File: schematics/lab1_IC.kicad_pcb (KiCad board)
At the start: 2 copper layers, 67.1 x 68.6 mm, 19 parts, among them J1 Barrel_Jack, M1 Motor_Servo, U1 LM7805_TO220, U2 NodeMCU, U3 DHT11

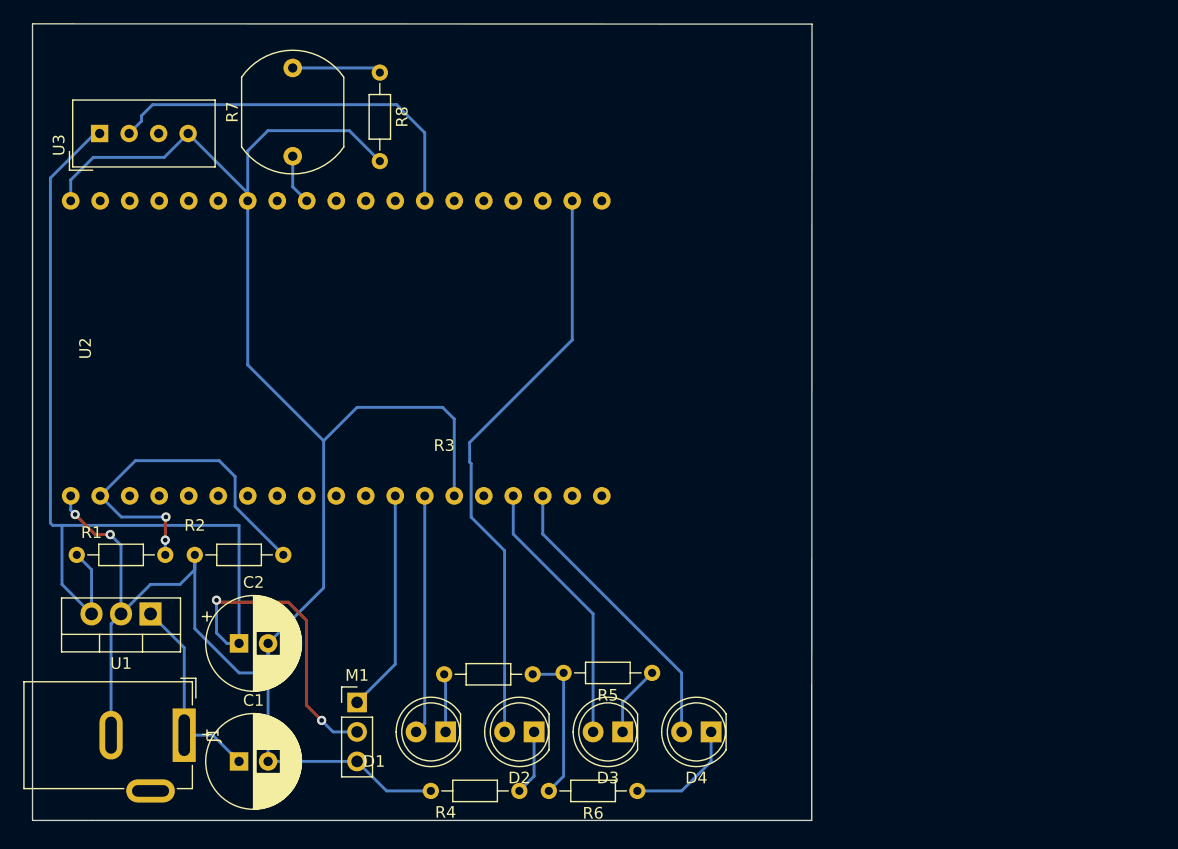
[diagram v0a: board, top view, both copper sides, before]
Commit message: added: servo functions to firmware
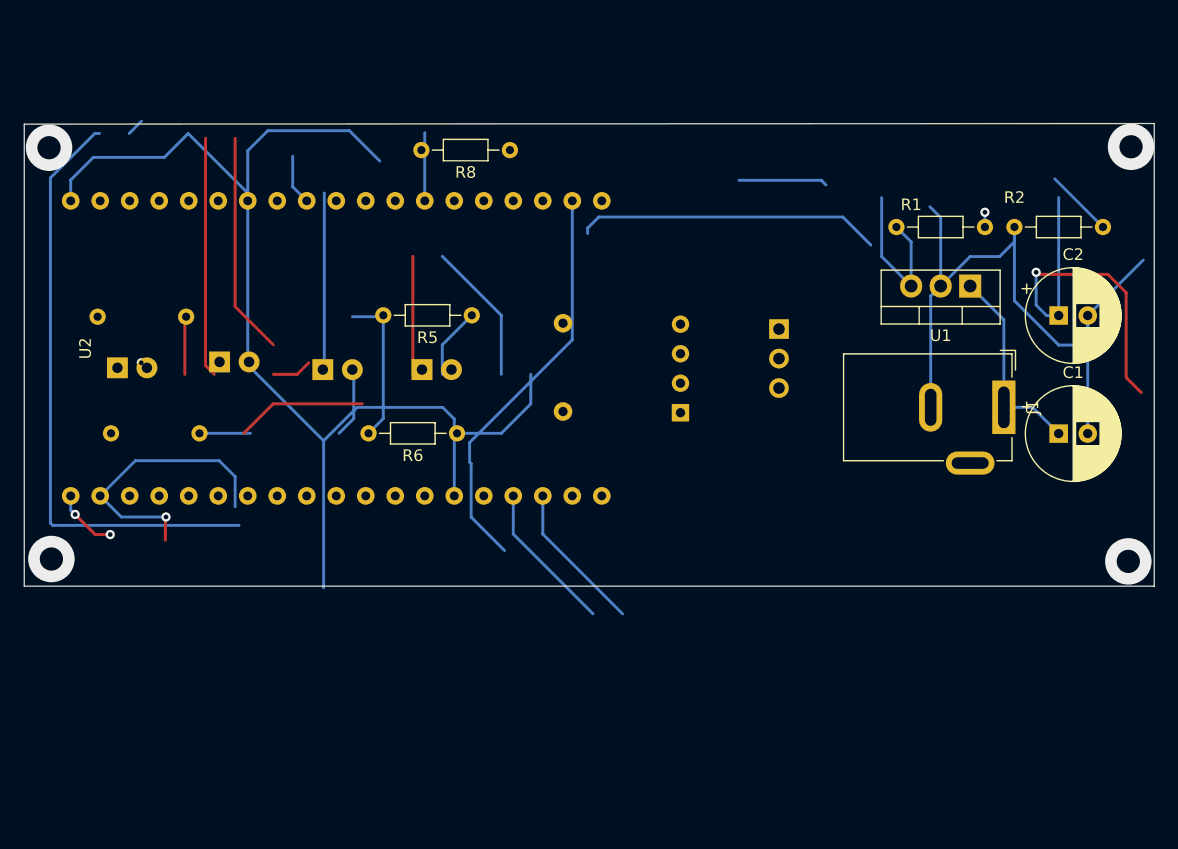
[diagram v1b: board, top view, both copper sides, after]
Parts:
- D1, D2, D3, D4, M1, R3, R4, R7, U3: moved to B.Cu
- moved U1 76.0 mm to (179.8, 88.6)
- moved C1 76.0 mm to (187.4, 101.3)
- moved C2 76.0 mm to (187.4, 91.2)
- moved J1 76.0 mm to (182.7, 99.1)
- moved R1 76.0 mm to (173.4, 83.5)
- moved R2 76.0 mm to (191.2, 83.5)
- moved U3 55.5 mm to (154.8, 99.5), turned to 0 degrees
- moved M1 48.5 mm to (163.3, 92.3), turned to 180 degrees
- moved R4 46.7 mm to (105.8, 101.3), turned to 0 degrees
- moved D1 42.2 mm to (106.4, 95.7), turned to 0 degrees
- moved D2 41.8 mm to (115.2, 95.1), turned to 0 degrees
- moved D3 40.5 mm to (124.1, 95.8), turned to 0 degrees
- moved D4 39.9 mm to (132.6, 95.8), turned to 0 degrees
- moved R3 38.0 mm to (112.3, 91.3), turned to 180 degrees
- moved R6 34.5 mm to (135.6, 101.3)
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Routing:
- net Net-(D3-Pad1): track 6.13 -> 21.7 mm
- net SERVO_LED1: track 50.6 -> 35.0 mm
- net Net-(D4-Pad1): track 9.94 -> 20.1 mm
- net Net-(D2-Pad1): track 5.61 -> 0.00 mm
- net P1_LED: track 23.2 -> 18.6 mm
- net 5V: vias 2 -> 1
- net SERVO_LED2: vias 0 -> 1
- net (no net): vias 0 -> 4
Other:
- board size 67.1 x 68.6 mm -> 97.3 x 39.8 mm
